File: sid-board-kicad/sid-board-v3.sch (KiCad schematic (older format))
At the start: 41 parts, among them J1 SPI+IRQ+POWER, J2 USB_B_Micro, SW1 SW_EN, SW2 SW_FLASH, U1 SC16IS752IPW, U2 MCP1703A-3302_SOT223, U3 SN65HVD232, U4 SN65HVD232, U5 MCP1703A-5002_SOT223, U6 ESP32-WROOM-32U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

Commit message: Assigned basic footprints
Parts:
- C2: footprint (none) -> Capacitor_SMD:C_0805_2012Metric_Pad1.15x1.40mm_HandSolder
- R2, R3, R4, R5: footprint (none) -> Resistor_SMD:R_0805_2012Metric_Pad1.15x1.40mm_HandSolder
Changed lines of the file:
@@
 F 0 "R4" V 7904 5150 50  0000 C CNN
 F 1 "10k" V 7995 5150 50  0000 C CNN
-F 2 "" H 8100 5150 50  0001 C CNN
+F 2 "Resistor_SMD:R_0805_2012Metric_Pad1.15x1.40mm_HandSolder" H 8100 5150 50  0001 C CNN
 F 3 "~" H 8100 5150 50  0001 C CNN
 	1    8100 5150
@@
 F 0 "R2" V 7704 5150 50  0000 C CNN
 F 1 "470" V 7795 5150 50  0000 C CNN
-F 2 "" H 7900 5150 50  0001 C CNN
+F 2 "Resistor_SMD:R_0805_2012Metric_Pad1.15x1.40mm_HandSolder" H 7900 5150 50  0001 C CNN
 F 3 "~" H 7900 5150 50  0001 C CNN
 	1    7900 5150
@@
 F 0 "C2" V 5675 3650 50  0000 C CNN
 F 1 "100uF" V 5766 3650 50  0000 C CNN
-F 2 "" H 5900 3650 50  0001 C CNN
+F 2 "Capacitor_SMD:C_0805_2012Metric_Pad1.15x1.40mm_HandSolder" H 5900 3650 50  0001 C CNN
 F 3 "~" H 5900 3650 50  0001 C CNN
 	1    5900 3650
@@
 F 0 "R5" V 7904 5600 50  0000 C CNN
 F 1 "10k" V 7995 5600 50  0000 C CNN
-F 2 "" H 8100 5600 50  0001 C CNN
+F 2 "Resistor_SMD:R_0805_2012Metric_Pad1.15x1.40mm_HandSolder" H 8100 5600 50  0001 C CNN
 F 3 "~" H 8100 5600 50  0001 C CNN
 	1    8100 5600
@@
 F 0 "R3" V 7704 5600 50  0000 C CNN
 F 1 "470" V 7795 5600 50  0000 C CNN
-F 2 "" H 7900 5600 50  0001 C CNN
+F 2 "Resistor_SMD:R_0805_2012Metric_Pad1.15x1.40mm_HandSolder" H 7900 5600 50  0001 C CNN
 F 3 "~" H 7900 5600 50  0001 C CNN
 	1    7900 5600

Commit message: Added UART interface to the SID BOARD V3
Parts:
- removed C2: 100uF, Capacitor_SMD:C_0805_2012Metric_Pad1.15x1.40mm_HandSolder, symbol Device:CP_Small
- removed R11, R12, R13, R14, R15, R16, R17: 1K, Resistor_SMD:R_0805_2012Metric_Pad1.15x1.40mm_HandSolder, symbol Device:R_Small
- removed U5: MCP1703A-5002_SOT223, Package_TO_SOT_SMD:SOT-223-3_TabPin2, symbol Regulator_Linear:MCP1703A-5002_SOT223
- added C10, C7: 10uF, Capacitor_Tantalum_SMD:CP_EIA-6032-20_AVX-F_Pad2.25x2.35mm_HandSolder, symbol Device:C_Small
- added C11, C2, C3, C5, C6, C8, C9: 1uF, Capacitor_SMD:C_0805_2012Metric_Pad1.15x1.40mm_HandSolder, symbol Device:C_Small
- added D11: 1N5819, Diode_SMD:D_SOD-123, symbol Diode:1N5819
- added D12, D13: LED0, LED_SMD:LED_0805_2012Metric_Pad1.15x1.40mm_HandSolder, symbol Device:LED
- added J3: UART, Connector_PinSocket_2.54mm:PinSocket_2x04_P2.54mm_Vertical, symbol Connector_Generic:Conn_02x04_Counter_Clockwise
- added Q1, Q2: BSS138, Package_TO_SOT_SMD:SOT-23, symbol Transistor_FET:BSS138
- added R7, R8: 1k, Resistor_SMD:R_0805_2012Metric_Pad1.15x1.40mm_HandSolder, symbol Device:R_Small
- added U5: CY7C65213-28PVXI, Package_SO:SSOP-28_5.3x10.2mm_P0.65mm, symbol Interface_USB:CY7C65213-28PVXI
- C1, C4: value 0.1uF -> 1uF
- J1: value SPI+IRQ+POWER -> SPI + UART
- R4, R5: value 10k -> 1k
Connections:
- net labels added: DTR, RI, RTS, RX_ESP32, SLEEP, TX_ESP32, USB_DM, USB_DP, VBUS
- net labels removed: VDD_5V
- wire segments 32 -> 65
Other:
- note added: "ESP32 MODULE"
- note removed: "5V SUPPLY LDO"
- moved on the sheet: D1, D10, D2, D3, D4, D5, D6, D7, D8, D9, J1, J2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

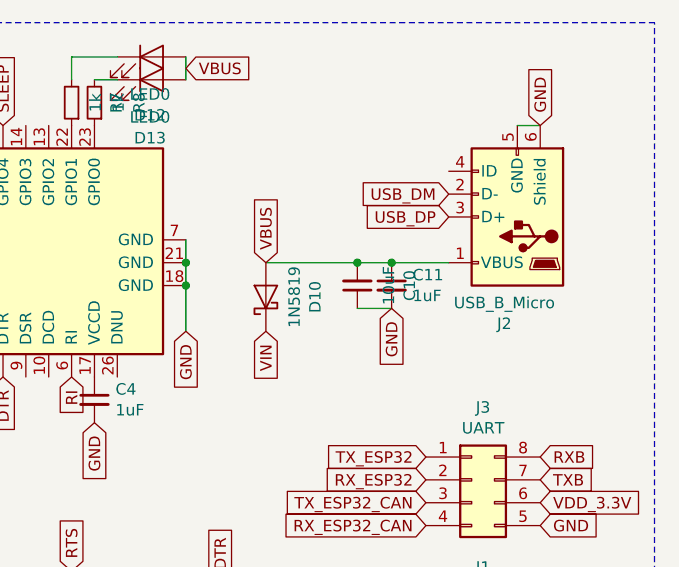
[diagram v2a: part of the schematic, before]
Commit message: Initial grouped PCB layout
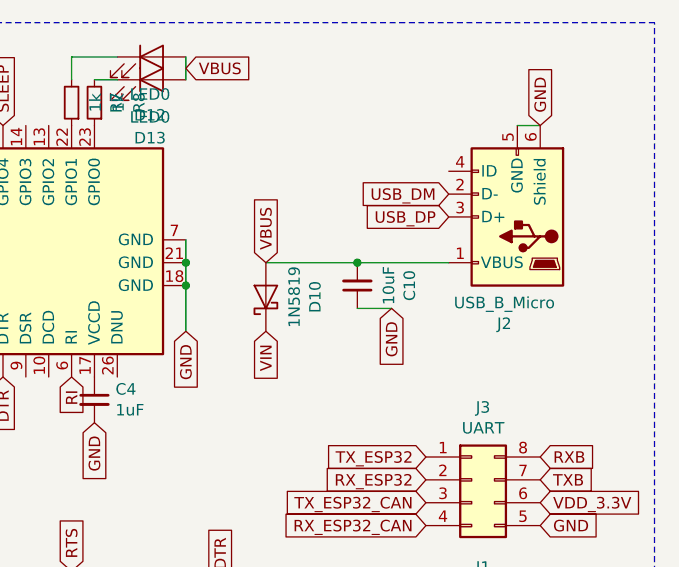
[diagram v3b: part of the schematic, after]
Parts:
- removed C11: 1uF, Capacitor_SMD:C_0805_2012Metric_Pad1.15x1.40mm_HandSolder, symbol Device:C_Small
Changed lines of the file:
@@
 $EndDescr
-$Comp
-L local_symbols:SC16IS752IPW_SPI U1
-U 1 1 5E1EA07F
-P 5400 1750
-F 0 "U1" H 5425 2665 50  0000 C CNN
-F 1 "SC16IS752IPW" H 5425 2574 50  0000 C CNN
-F 2 "Package_SO:TSSOP-28_4.4x9.7mm_P0.65mm" H 5400 850 50  0001 C CNN
-F 3 "https://au.mouser.com/datasheet/2/302/SC16IS752_SC16IS762-1127856.pdf" H 5200 1950 50  0001 C CNN
-	1    5400 1750
-	1    0    0    -1
-$EndComp
 $Comp
 L local_symbols:Conn_02x06_SAAB_SID_HPD ICM1
@@
 	7100 4250 7100 4150
 $Comp
-L Device:C_Small C11
-U 1 1 5F4AB75F
-P 9600 4350
-F 0 "C11" H 9692 4396 50  0000 L CNN
-F 1 "1uF" H 9692 4305 50  0000 L CNN
-F 2 "Capacitor_SMD:C_0805_2012Metric_Pad1.15x1.40mm_HandSolder" H 9600 4350 50  0001 C CNN
-F 3 "~" H 9600 4350 50  0001 C CNN
-	1    9600 4350
-	1    0    0    -1
-$EndComp
-$Comp
 L Device:C_Small C10
 U 1 1 5F4B4B6B
@@
 	9050 4250 9450 4250
 Connection ~ 9450 4250
-Wire Wire Line
-	9450 4250 9600 4250
-Connection ~ 9600 4250
-Wire Wire Line
-	9600 4250 9850 4250
 Text GLabel 9600 4450 3    50   Input ~ 0
 GND
@@
 Wire Notes Line
 	4300 3200 10750 3200
+$Comp
+L local_symbols:SC16IS752IPW_SPI U1
+U 1 1 5E1EA07F
+P 5400 1750
+F 0 "U1" H 5425 2665 50  0000 C CNN
+F 1 "SC16IS752IPW" H 5425 2574 50  0000 C CNN
+F 2 "Package_SO:TSSOP-28_4.4x9.7mm_P0.65mm" H 5400 850 50  0001 C CNN
+F 3 "https://au.mouser.com/datasheet/2/302/SC16IS752_SC16IS762-1127856.pdf" H 5200 1950 50  0001 C CNN
+	1    5400 1750
+	1    0    0    -1
+$EndComp
+Wire Wire Line
+	9450 4250 9850 4250
 $EndSCHEMATC

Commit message: Experimenting with PCB layouts
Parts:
- removed C10: 10uF, Capacitor_Tantalum_SMD:CP_EIA-6032-20_AVX-F_Pad2.25x2.35mm_HandSolder, symbol Device:C_Small
- added I-BUS1: Screw_Terminal_01x02, TerminalBlock_Phoenix:TerminalBlock_Phoenix_MKDS-1,5-2-5.08_1x02_P5.08mm_Horizontal, symbol Connector:Screw_Terminal_01x02
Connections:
- net CAN_H: now also I-BUS1.2 (Pin_2)
- net CAN_L: now also I-BUS1.1 (Pin_1)
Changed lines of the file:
@@
 Wire Wire Line
 	7100 4250 7100 4150
-$Comp
-L Device:C_Small C10
-U 1 1 5F4B4B6B
-P 9450 4350
-F 0 "C10" V 9221 4350 50  0000 C CNN
-F 1 "10uF" V 9312 4350 50  0000 C CNN
-F 2 "Capacitor_Tantalum_SMD:CP_EIA-6032-20_AVX-F_Pad2.25x2.35mm_HandSolder" H 9450 4350 50  0001 C CNN
-F 3 "~" H 9450 4350 50  0001 C CNN
-	1    9450 4350
-	-1   0    0    1
-$EndComp
-Wire Wire Line
-	9050 4250 9450 4250
-Connection ~ 9450 4250
-Text GLabel 9600 4450 3    50   Input ~ 0
-GND
-Wire Wire Line
-	9600 4450 9450 4450
 Text GLabel 8200 4750 3    50   Input ~ 0
 RI
@@
 	1    0    0    -1
 $EndComp
+$Comp
+L Connector:Screw_Terminal_01x02 I-BUS1
+U 1 1 5F317B0C
+P 1350 3700
+F 0 "I-BUS1" H 1430 3692 50  0000 L CNN
+F 1 "Screw_Terminal_01x02" H 1430 3601 50  0000 L CNN
+F 2 "TerminalBlock_Phoenix:TerminalBlock_Phoenix_MKDS-1,5-2-5.08_1x02_P5.08mm_Horizontal" H 1350 3700 50  0001 C CNN
+F 3 "~" H 1350 3700 50  0001 C CNN
+	1    1350 3700
+	1    0    0    -1
+$EndComp
+Text GLabel 1150 3700 0    50   Input ~ 0
+CAN_L
+Text GLabel 1150 3800 0    50   Input ~ 0
+CAN_H
 Wire Wire Line
-	9450 4250 9850 4250
+	9050 4250 9850 4250
 $EndSCHEMATC

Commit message: Crazy routing
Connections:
- net CAN_A_H: now also ICM1.10 (CAN_H); no longer ICM1.9 (CAN_L)
- net CAN_A_L: now also ICM1.9 (CAN_L); no longer ICM1.10 (CAN_H)
- net CAN_B_H: now also SID1.10 (CAN_H); no longer SID1.9 (CAN_L)
- net CAN_B_L: now also SID1.9 (CAN_L); no longer SID1.10 (CAN_H)
- net GND: now also C2.2, C5.2, U2.2 (GND)
- net RI: no longer names the net of U6.27 (IO16)
- net RI: no longer U5.6 (RI)
- net SLEEP: no longer names the net of U6.28 (IO17)
- net SLEEP: no longer U5.12 (GPIO4)
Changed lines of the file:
@@
 Text GLabel 3350 2900 0    50   Input ~ 0
 VDD_3.3V
-Text GLabel 1850 1400 2    50   Input ~ 0
+Text GLabel 1850 1500 2    50   Input ~ 0
 CAN_A_L
 Text GLabel 2950 1350 0    50   Input ~ 0
@@
 Text GLabel 2950 1450 0    50   Input ~ 0
 CAN_A_H
-Text GLabel 1850 1500 2    50   Input ~ 0
+Text GLabel 1850 1400 2    50   Input ~ 0
 CAN_A_H
+Text GLabel 1850 2400 2    50   Input ~ 0
+CAN_B_H
 Text GLabel 1850 2500 2    50   Input ~ 0
-CAN_B_H
-Text GLabel 1850 2400 2    50   Input ~ 0
 CAN_B_L
 Text GLabel 2950 2500 0    50   Input ~ 0
@@
 Wire Wire Line
 	7100 4250 7100 4150
-Text GLabel 8200 4750 3    50   Input ~ 0
-RI
-Text GLabel 5900 4850 2    50   Input ~ 0
-RI
-Text GLabel 7900 3650 1    50   Input ~ 0
-SLEEP
-Text GLabel 5900 4950 2    50   Input ~ 0
-SLEEP
 $Comp
 L Device:LED D12
@@
 Wire Wire Line
 	9050 4250 9850 4250
+Text GLabel 3300 5350 3    50   Input ~ 0
+GND
 $EndSCHEMATC

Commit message: Redid routing more logically
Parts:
- removed J3: UART, Connector_PinSocket_2.54mm:PinSocket_2x04_P2.54mm_Vertical, symbol Connector_Generic:Conn_02x04_Counter_Clockwise
- J1: footprint Connector_PinSocket_2.54mm:PinSocket_2x04_P2.54mm_Vertical -> Connector_PinHeader_1.00mm:PinHeader_2x05_P1.00mm_Vertical; symbol Connector_Generic:Conn_02x04_Counter_Clockwise -> Connector_Generic:Conn_02x05_Counter_Clockwise
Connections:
- net CAN_H: now also I-BUS1.1 (Pin_1); no longer I-BUS1.2 (Pin_2)
- net CAN_L: now also I-BUS1.2 (Pin_2); no longer I-BUS1.1 (Pin_1)
- net CLK: now also J1.4 (Pin_4); no longer J1.2 (Pin_2)
- net GND: now also J1.10 (Pin_10), J1.6 (Pin_6), J1.8 (Pin_8); no longer J1.5 (Pin_5)
- net MISO: now also J1.3 (Pin_3); no longer J1.4 (Pin_4)
- net MOSI: now also J1.2 (Pin_2); no longer J1.3 (Pin_3)
- net RXA: no longer J1.8 (Pin_8)
- net TXA: no longer J1.7 (Pin_7)
- net VDD_3.3V: now also J1.5 (Pin_5), J1.7 (Pin_7), J1.9 (Pin_9); no longer J1.6 (Pin_6)
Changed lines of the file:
@@
 Text GLabel 10250 6100 2    50   Input ~ 0
 GND
-Text GLabel 10250 6000 2    50   Input ~ 0
+Text GLabel 9750 6100 0    50   Input ~ 0
 VDD_3.3V
 Text GLabel 4800 1900 0    50   Input ~ 0
@@
 Text GLabel 4850 2000 0    50   Input ~ 0
 CS
+Text GLabel 9750 6000 0    50   Input ~ 0
+CLK
 Text GLabel 9750 5900 0    50   Input ~ 0
-CLK
-Text GLabel 9750 6100 0    50   Input ~ 0
 MISO
-Text GLabel 9750 6000 0    50   Input ~ 0
+Text GLabel 9750 5800 0    50   Input ~ 0
 MOSI
-Text GLabel 9750 5800 0    50   Input ~ 0
+Text GLabel 9750 5700 0    50   Input ~ 0
 CS
 $Comp
-L Connector_Generic:Conn_02x04_Counter_Clockwise J1
+L Connector_Generic:Conn_02x05_Counter_Clockwise J1
 U 1 1 5E4709DB
 P 9950 5900
 F 0 "J1" H 10000 6217 50  0000 C CNN
 F 1 "SPI + UART" H 10000 6126 50  0000 C CNN
-F 2 "Connector_PinSocket_2.54mm:PinSocket_2x04_P2.54mm_Vertical" H 9950 5900 50  0001 C CNN
+F 2 "Connector_PinHeader_1.00mm:PinHeader_2x05_P1.00mm_Vertical" H 9950 5900 50  0001 C CNN
 F 3 "~" H 9950 5900 50  0001 C CNN
 	1    9950 5900
@@
 	1    0    0    -1
 $EndComp
-Text GLabel 10250 5400 2    50   Input ~ 0
-GND
-Text GLabel 10250 5300 2    50   Input ~ 0
-VDD_3.3V
-$Comp
-L Connector_Generic:Conn_02x04_Counter_Clockwise J3
-U 1 1 5F517DB1
-P 9950 5200
-F 0 "J3" H 10000 5517 50  0000 C CNN
-F 1 "UART" H 10000 5426 50  0000 C CNN
-F 2 "Connector_PinSocket_2.54mm:PinSocket_2x04_P2.54mm_Vertical" H 9950 5200 50  0001 C CNN
-F 3 "~" H 9950 5200 50  0001 C CNN
-	1    9950 5200
-	1    0    0    -1
-$EndComp
-Text GLabel 9750 5100 0    50   Input ~ 0
-TX_ESP32
-Text GLabel 9750 5200 0    50   Input ~ 0
-RX_ESP32
-Text GLabel 9750 5300 0    50   Input ~ 0
-TX_ESP32_CAN
-Text GLabel 9750 5400 0    50   Input ~ 0
-RX_ESP32_CAN
-Text GLabel 10250 5100 2    50   Input ~ 0
-RXB
-Text GLabel 10250 5200 2    50   Input ~ 0
-TXB
-Text GLabel 10250 5800 2    50   Input ~ 0
-RXA
-Text GLabel 10250 5900 2    50   Input ~ 0
-TXA
 Wire Notes Line
 	6150 6600 6150 6400
@@
 	1    0    0    -1
 $EndComp
+Wire Wire Line
+	9050 4250 9850 4250
+Text GLabel 3300 5350 3    50   Input ~ 0
+GND
+Text GLabel 1150 3700 0    50   Input ~ 0
+CAN_H
+Text GLabel 1150 3800 0    50   Input ~ 0
+CAN_L
 $Comp
 L Connector:Screw_Terminal_01x02 I-BUS1
@@
 	1    0    0    -1
 $EndComp
-Text GLabel 1150 3700 0    50   Input ~ 0
-CAN_L
-Text GLabel 1150 3800 0    50   Input ~ 0
-CAN_H
-Wire Wire Line
-	9050 4250 9850 4250
-Text GLabel 3300 5350 3    50   Input ~ 0
-GND
+Text GLabel 10250 5900 2    50   Input ~ 0
+GND
+Text GLabel 10250 5700 2    50   Input ~ 0
+GND
+Text GLabel 10250 5800 2    50   Input ~ 0
+VDD_3.3V
+Text GLabel 10250 6000 2    50   Input ~ 0
+VDD_3.3V
 $EndSCHEMATC

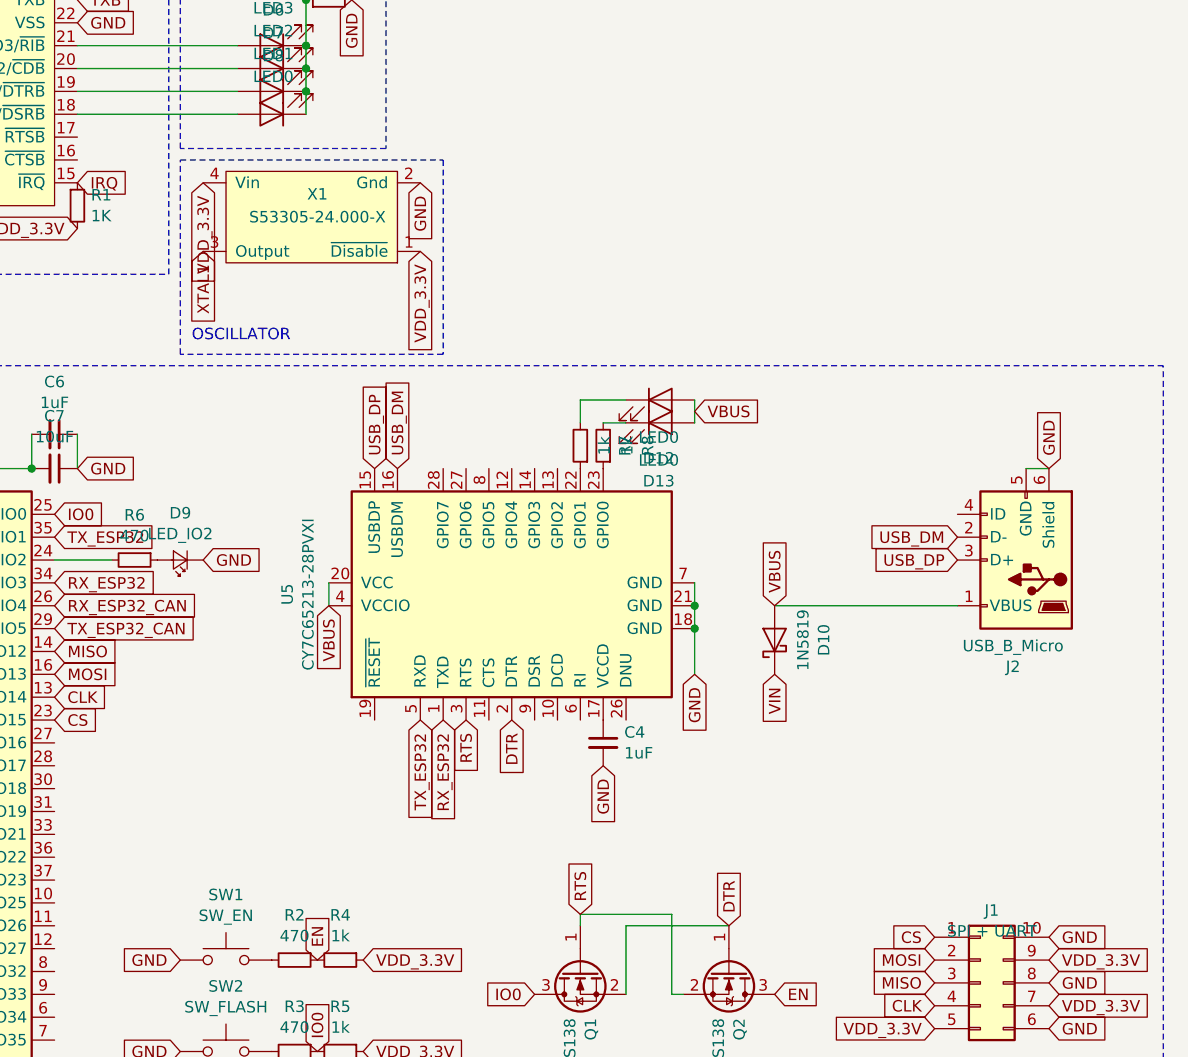
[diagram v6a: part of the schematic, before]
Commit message: Happy with routing, replaced oscillator, need to label.
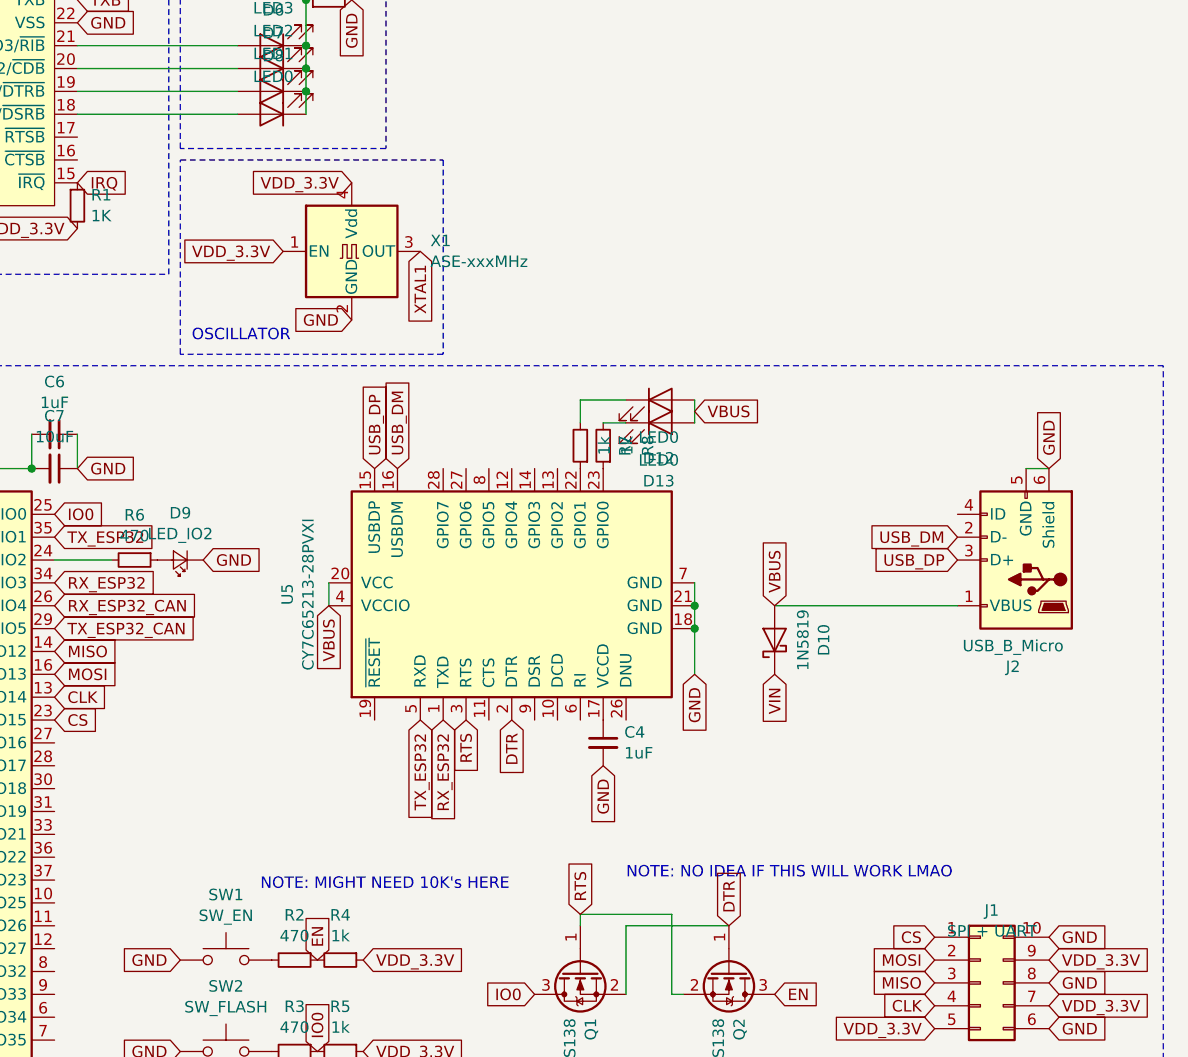
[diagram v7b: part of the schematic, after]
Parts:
- removed X1: S53305-24.000-X, sid-board:S53305-16.000-X, symbol local_symbols:S53305-16.000-X
- added X1: ASE-xxxMHz, Oscillator:Oscillator_SMD_EuroQuartz_XO53-4Pin_5.0x3.2mm_HandSoldering, symbol Oscillator:ASE-xxxMHz
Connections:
- net GND: now also X1.2 (GND)
- net VDD_3.3V: now also X1.1 (EN), X1.4 (Vdd)
- net XTAL1: now also X1.3 (OUT)
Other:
- note added: "NOTE: MIGHT NEED 10K's HERE"
- note added: "NOTE: NO IDEA IF THIS WILL WORK LMAO"
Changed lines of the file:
@@
 Text Notes 6500 3100 0    50   ~ 0
 OSCILLATOR
-Text GLabel 6550 2700 3    50   Input ~ 0
+Text GLabel 7500 2700 3    50   Input ~ 0
 XTAL1
-Text GLabel 7500 2400 3    50   Input ~ 0
+Text GLabel 7200 3000 0    50   Input ~ 0
 GND
 $Comp
@@
 Wire Notes Line
 	4300 850  6400 850
-$Comp
-L local_symbols:S53305-16.000-X X1
-U 1 1 5E7AFB1C
-P 7050 2600
-F 0 "X1" H 7050 2450 50  0000 C CNN
-F 1 "S53305-24.000-X" H 7050 2550 50  0000 C CNN
-F 2 "sid-board:S53305-16.000-X" H 7050 2600 50  0001 C CNN
-F 3 "" H 7050 2600 50  0001 C CNN
-	1    7050 2600
-	-1   0    0    1
-$EndComp
-Text GLabel 6550 2400 3    50   Input ~ 0
-VDD_3.3V
-Text GLabel 7500 2700 3    50   Input ~ 0
+Text GLabel 6900 2700 0    50   Input ~ 0
+VDD_3.3V
+Text GLabel 7200 2400 0    50   Input ~ 0
 VDD_3.3V
 Wire Notes Line
@@
 Text GLabel 10250 6000 2    50   Input ~ 0
 VDD_3.3V
+Text Notes 6800 5500 0    50   ~ 0
+NOTE: MIGHT NEED 10K's HERE
+Text Notes 8400 5450 0    50   ~ 0
+NOTE: NO IDEA IF THIS WILL WORK LMAO
+$Comp
+L Oscillator:ASE-xxxMHz X1
+U 1 1 5F3441C0
+P 7200 2700
+F 0 "X1" H 7544 2746 50  0000 L CNN
+F 1 "ASE-xxxMHz" H 7544 2655 50  0000 L CNN
+F 2 "Oscillator:Oscillator_SMD_EuroQuartz_XO53-4Pin_5.0x3.2mm_HandSoldering" H 7900 2350 50  0001 C CNN
+F 3 "http://www.abracon.com/Oscillators/ASV.pdf" H 7100 2700 50  0001 C CNN
+	1    7200 2700
+	1    0    0    -1
+$EndComp
 $EndSCHEMATC
